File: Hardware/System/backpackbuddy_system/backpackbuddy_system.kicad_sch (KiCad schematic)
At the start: 27 parts, among them J1 PIR, J2 Ultrasonic 2, J3 Ultrasonic 1, J4 Left Vibration 1, J5 Left Vibration 2, J6 Raspberry Pi, J7 ESP8266, J8 Right Vibration 1, J9 Right Vibration 2, Q1 Q_NMOS_GSD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

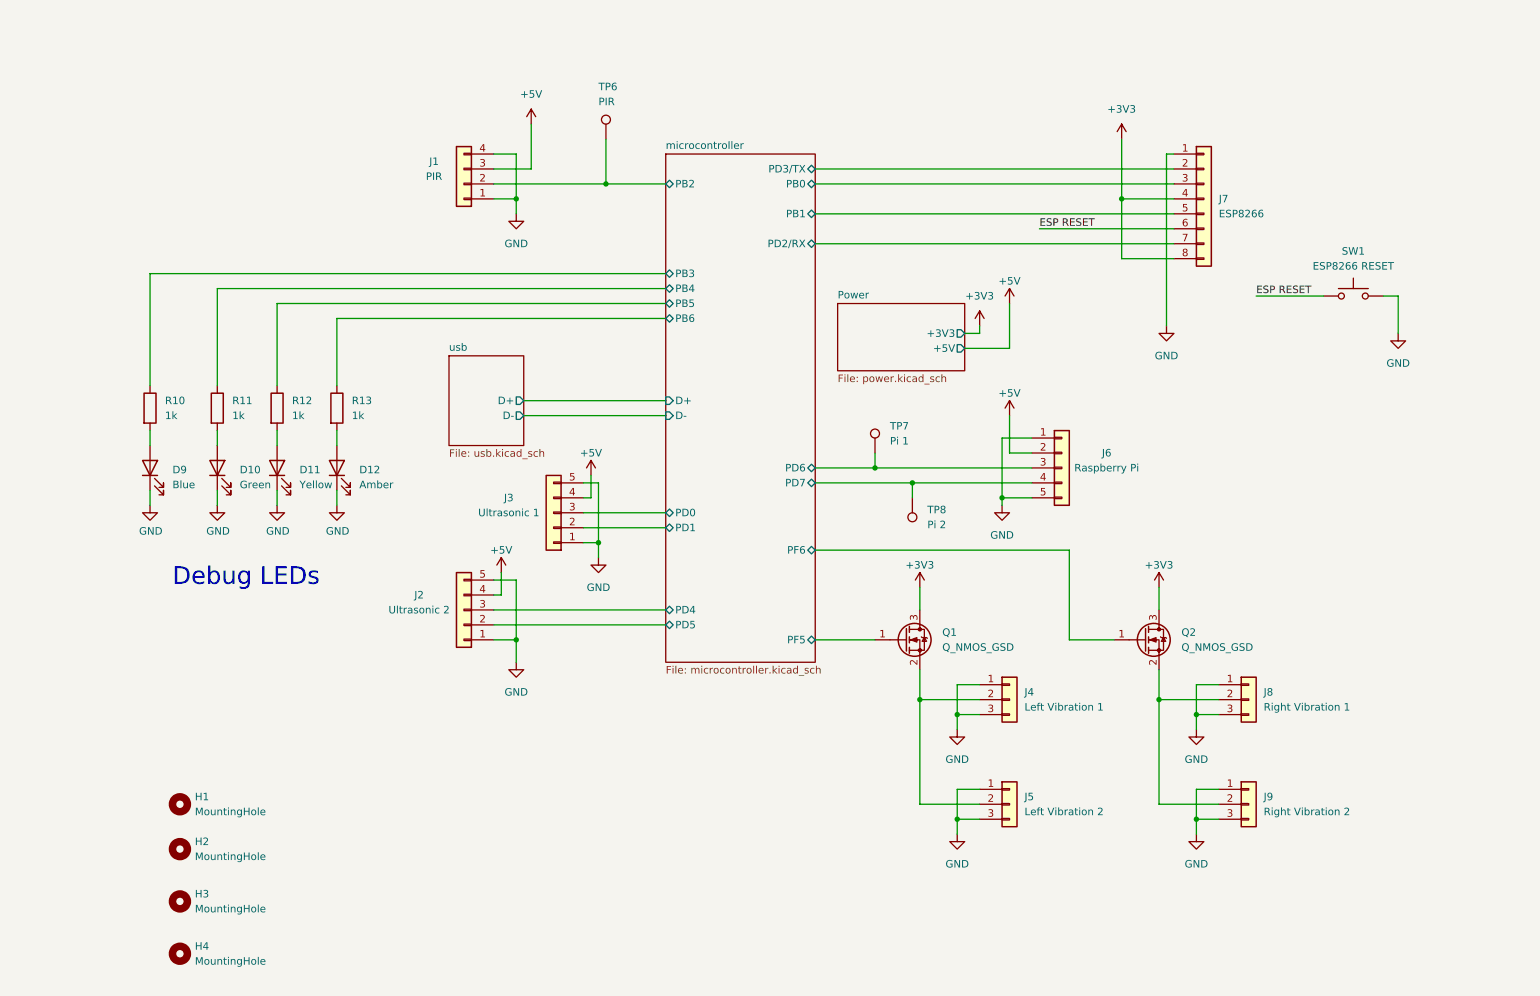
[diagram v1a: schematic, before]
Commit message: about to go crazy with the raspberry pi setup on schematic then will layout after dinner hehe
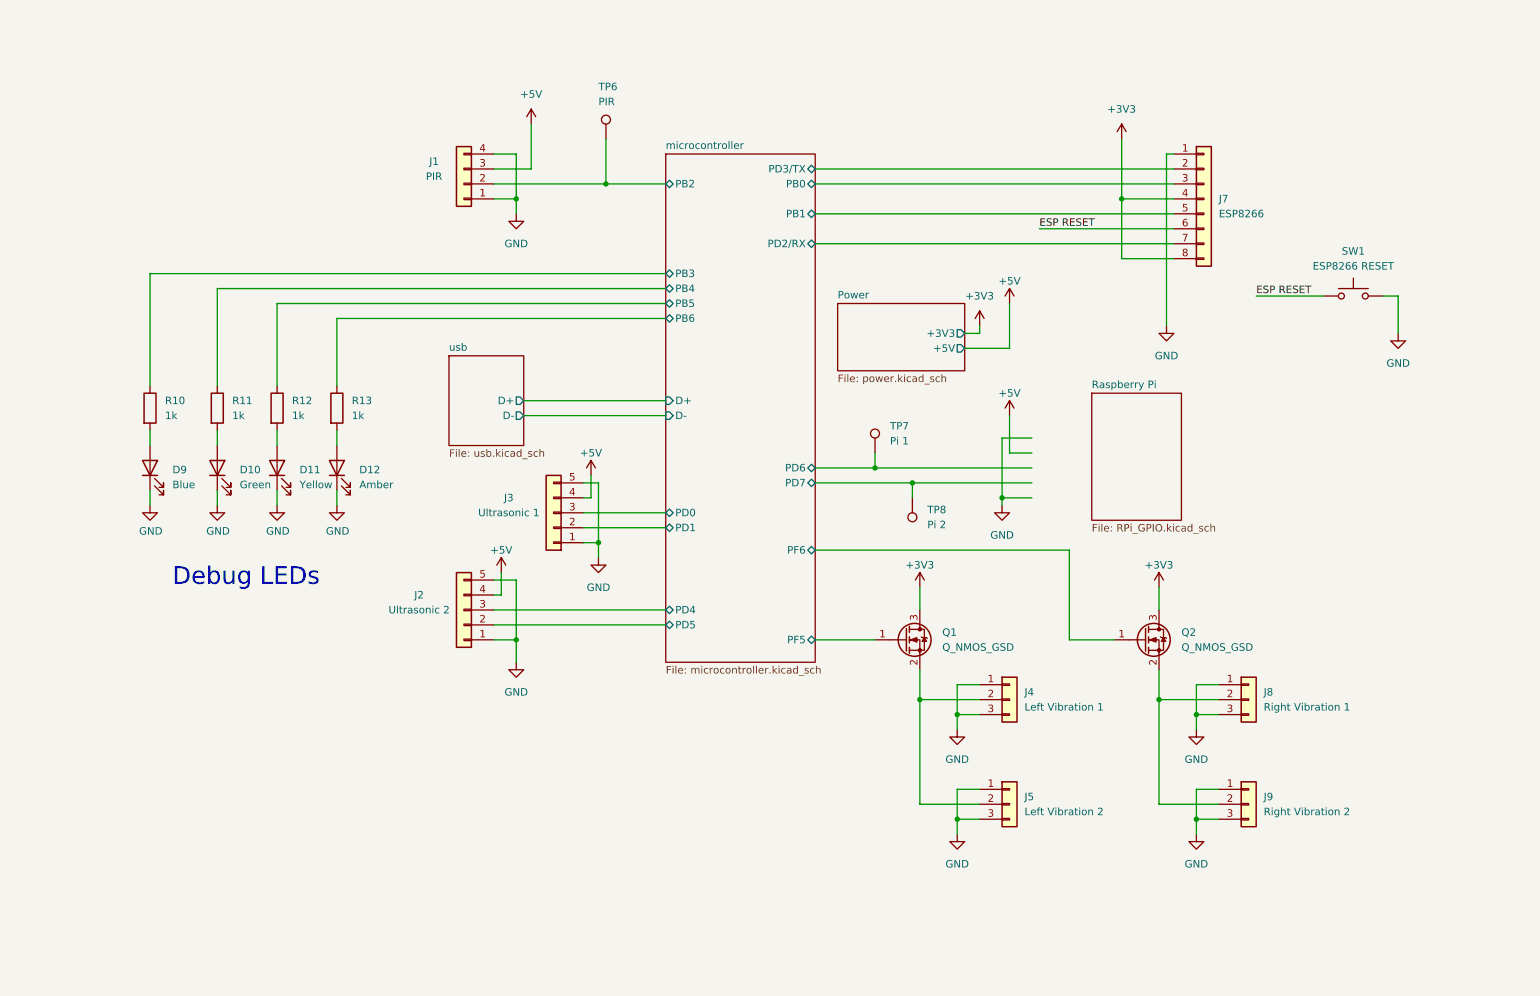
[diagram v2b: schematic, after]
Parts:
- removed H1, H2, H3, H4: MountingHole, MountingHole:MountingHole_2.7mm_M2.5, symbol Mechanical:MountingHole
- removed J6: Raspberry Pi, Connector_PinHeader_2.54mm:PinHeader_1x05_P2.54mm_Vertical, symbol Connector_Generic:Conn_01x05
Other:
- added sheet Raspberry Pi (RPi_GPIO.kicad_sch)
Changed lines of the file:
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@@
     (pin "1")
-  )
-  (symbol (lib_id "Mechanical:MountingHole") (at 49.53 156.21 0) (unit 1)
-    (in_bom yes) (on_board yes) (fields_autoplaced)
-    (property "Reference" "H2" (id 0) (at 52.07 154.9399 0)
-      (effects (font (size 1.27 1.27)) (justify left))
-    )
-    (property "Value" "MountingHole" (id 1) (at 52.07 157.4799 0)
-      (effects (font (size 1.27 1.27)) (justify left))
-    )
-    (property "Footprint" "MountingHole:MountingHole_2.7mm_M2.5" (id 2) (at 49.53 156.21 0)
-      (effects (font (size 1.27 1.27)) hide)
-    )
-    (property "Datasheet" "~" (id 3) (at 49.53 156.21 0)
-      (effects (font (size 1.27 1.27)) hide)
-    )
   )
   (symbol (lib_id "power:GND") (at 66.04 97.79 0) (unit 1)
@@
     (pin "1")
   )
-  (symbol (lib_id "Mechanical:MountingHole") (at 49.53 165.1 0) (unit 1)
-    (in_bom yes) (on_board yes) (fields_autoplaced)
-    (property "Reference" "H3" (id 0) (at 52.07 163.8299 0)
-      (effects (font (size 1.27 1.27)) (justify left))
-    )
-    (property "Value" "MountingHole" (id 1) (at 52.07 166.3699 0)
-      (effects (font (size 1.27 1.27)) (justify left))
-    )
-    (property "Footprint" "MountingHole:MountingHole_2.7mm_M2.5" (id 2) (at 49.53 165.1 0)
-      (effects (font (size 1.27 1.27)) hide)
-    )
-    (property "Datasheet" "~" (id 3) (at 49.53 165.1 0)
-      (effects (font (size 1.27 1.27)) hide)
-    )
-  )
   (symbol (lib_id "Device:R") (at 76.2 81.28 0) (unit 1)
     (in_bom yes) (on_board yes) (fields_autoplaced)
@@
     (pin "1")
   )
-  (symbol (lib_id "Mechanical:MountingHole") (at 49.53 173.99 0) (unit 1)
-    (in_bom yes) (on_board yes) (fields_autoplaced)
-    (property "Reference" "H4" (id 0) (at 52.07 172.7199 0)
-      (effects (font (size 1.27 1.27)) (justify left))
-    )
-    (property "Value" "MountingHole" (id 1) (at 52.07 175.2599 0)
-      (effects (font (size 1.27 1.27)) (justify left))
-    )
-    (property "Footprint" "MountingHole:MountingHole_2.7mm_M2.5" (id 2) (at 49.53 173.99 0)
-      (effects (font (size 1.27 1.27)) hide)
-    )
-    (property "Datasheet" "~" (id 3) (at 49.53 173.99 0)
-      (effects (font (size 1.27 1.27)) hide)
-    )
-  )
   (symbol (lib_id "power:+5V") (at 104.14 109.22 0) (unit 1)
     (in_bom yes) (on_board yes)
@@
     (pin "1")
   )
-  (symbol (lib_id "Mechanical:MountingHole") (at 49.53 148.59 0) (unit 1)
-    (in_bom yes) (on_board yes) (fields_autoplaced)
-    (property "Reference" "H1" (id 0) (at 52.07 147.3199 0)
-      (effects (font (size 1.27 1.27)) (justify left))
-    )
-    (property "Value" "MountingHole" (id 1) (at 52.07 149.8599 0)
-      (effects (font (size 1.27 1.27)) (justify left))
-    )
-    (property "Footprint" "MountingHole:MountingHole_2.7mm_M2.5" (id 2) (at 49.53 148.59 0)
-      (effects (font (size 1.27 1.27)) hide)
-    )
-    (property "Datasheet" "~" (id 3) (at 49.53 148.59 0)
-      (effects (font (size 1.27 1.27)) hide)
-    )
-  )
   (symbol (lib_id "power:GND") (at 181.61 153.67 0) (unit 1)
     (in_bom yes) (on_board yes) (fields_autoplaced)
@@
     )
     (pin "1")
-  )
-  (symbol (lib_id "Connector_Generic:Conn_01x05") (at 199.39 91.44 0) (unit 1)
-    (in_bom yes) (on_board yes)
-    (property "Reference" "J6" (id 0) (at 207.01 88.9 0))
-    (property "Value" "Raspberry Pi" (id 1) (at 207.01 91.44 0))
-    (property "Footprint" "Connector_PinHeader_2.54mm:PinHeader_1x05_P2.54mm_Vertical" (id 2) (at 199.39 91.44 0)
-      (effects (font (size 1.27 1.27)) hide)
-    )
-    (property "Datasheet" "~" (id 3) (at 199.39 91.44 0)
-      (effects (font (size 1.27 1.27)) hide)
-    )
-    (property "Stock" "In connector kit" (id 4) (at 199.39 91.44 0)
-      (effects (font (size 1.27 1.27)) hide)
-    )
-    (pin "1")
-    (pin "2")
-    (pin "3")
-    (pin "4")
-    (pin "5")
   )
   (symbol (lib_id "power:+3V3") (at 215.9 111.76 0) (unit 1)
@@
     )
   )
+  (sheet (at 204.47 78.74) (size 15.24 21.59) (fields_autoplaced)
+    (stroke (width 0.1524) (type solid) (color 0 0 0 0))
+    (fill (color 0 0 0 0.0000))
+    (property "Sheet name" "Raspberry Pi" (id 0) (at 204.47 78.0284 0)
+      (effects (font (size 1.27 1.27)) (justify left bottom))
+    )
+    (property "Sheet file" "RPi_GPIO.kicad_sch" (id 1) (at 204.47 100.9146 0)
+      (effects (font (size 1.27 1.27)) (justify left top))
+    )
+  )
   (sheet (at 95.25 72.39) (size 12.7 15.24) (fields_autoplaced)
     (stroke (width 0.1524) (type solid) (color 0 0 0 0))
@@
     (path "/cf3dbeef-e165-4b09-9181-2cdb640e2044" (page "3"))
     (path "/31ba9691-809e-422e-95e0-c0a31dc5a8d2" (page "4"))
+    (path "/b75bd9b9-3a6b-4766-98aa-3c30f703f2e0" (page "5"))
   )
   (symbol_instances
@@
       (reference "F2") (unit 1) (value "4A") (footprint "Fuse:Fuse_0603_1608Metric_Pad1.05x0.95mm_HandSolder")
     )
-    (path "/7ba4c5ab-53c8-4ed6-a56b-d48ce55bed3f"
-      (reference "H1") (unit 1) (value "MountingHole") (footprint "MountingHole:MountingHole_2.7mm_M2.5")
-    )
-    (path "/2e721548-39f6-4c3c-af59-f1b3c0cd0ccf"
-      (reference "H2") (unit 1) (value "MountingHole") (footprint "MountingHole:MountingHole_2.7mm_M2.5")
-    )
-    (path "/3f16932f-c1ad-452a-a9d6-eed8bdfe8267"
-      (reference "H3") (unit 1) (value "MountingHole") (footprint "MountingHole:MountingHole_2.7mm_M2.5")
-    )
-    (path "/6b7cec68-8bf5-4c72-bd57-d348fd442c4a"
-      (reference "H4") (unit 1) (value "MountingHole") (footprint "MountingHole:MountingHole_2.7mm_M2.5")
-    )
     (path "/e1c39392-4fee-4a21-be8c-0ca37da1cb84"
       (reference "J1") (unit 1) (value "PIR") (footprint "Connector_PinHeader_2.54mm:PinHeader_1x04_P2.54mm_Vertical")
@@
       (reference "J5") (unit 1) (value "Left Vibration 2") (footprint "Connector_PinHeader_2.54mm:PinHeader_1x03_P2.54mm_Vertical")
     )
-    (path "/9f3434b7-25eb-451d-ae48-b1d6349ea6b5"
-      (reference "J6") (unit 1) (value "Raspberry Pi") (footprint "Connector_PinHeader_2.54mm:PinHeader_1x05_P2.54mm_Vertical")
+    (path "/b75bd9b9-3a6b-4766-98aa-3c30f703f2e0/680f5a3d-03b5-4375-afa9-99b8f3b6f5b5"
+      (reference "J6") (unit 1) (value "RPi_GPIO") (footprint "")
     )
     (path "/d8ba2266-3fc9-4f5f-8bd8-53203e01ee14"

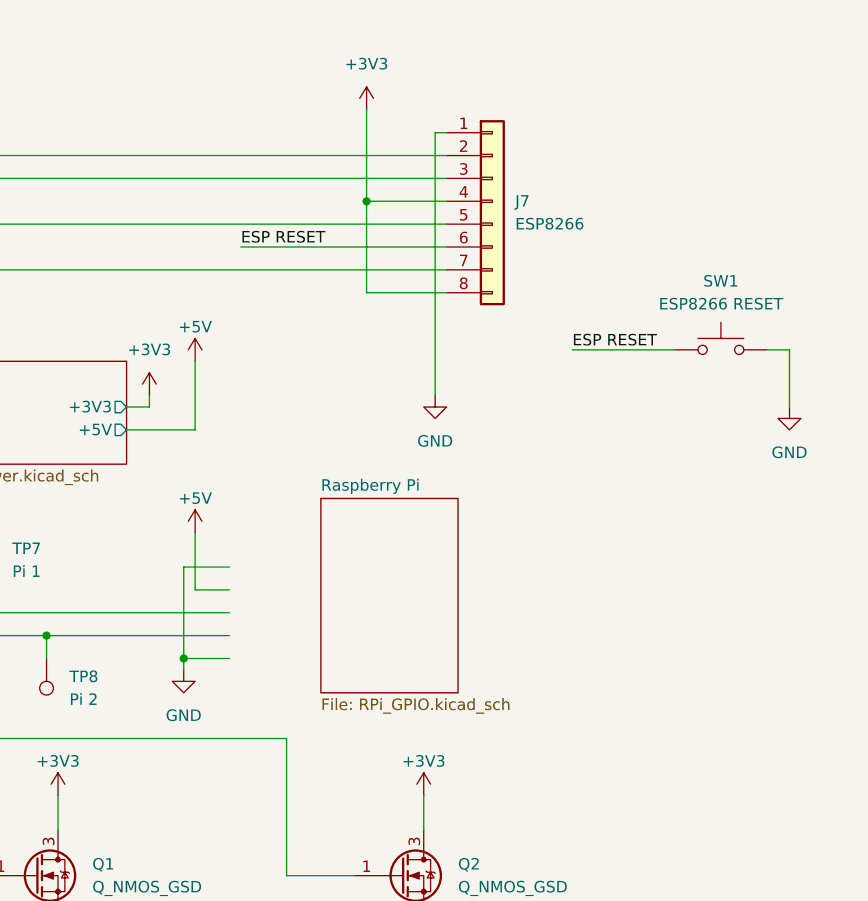
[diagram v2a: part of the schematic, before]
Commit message: pull down resistor to ESP reset
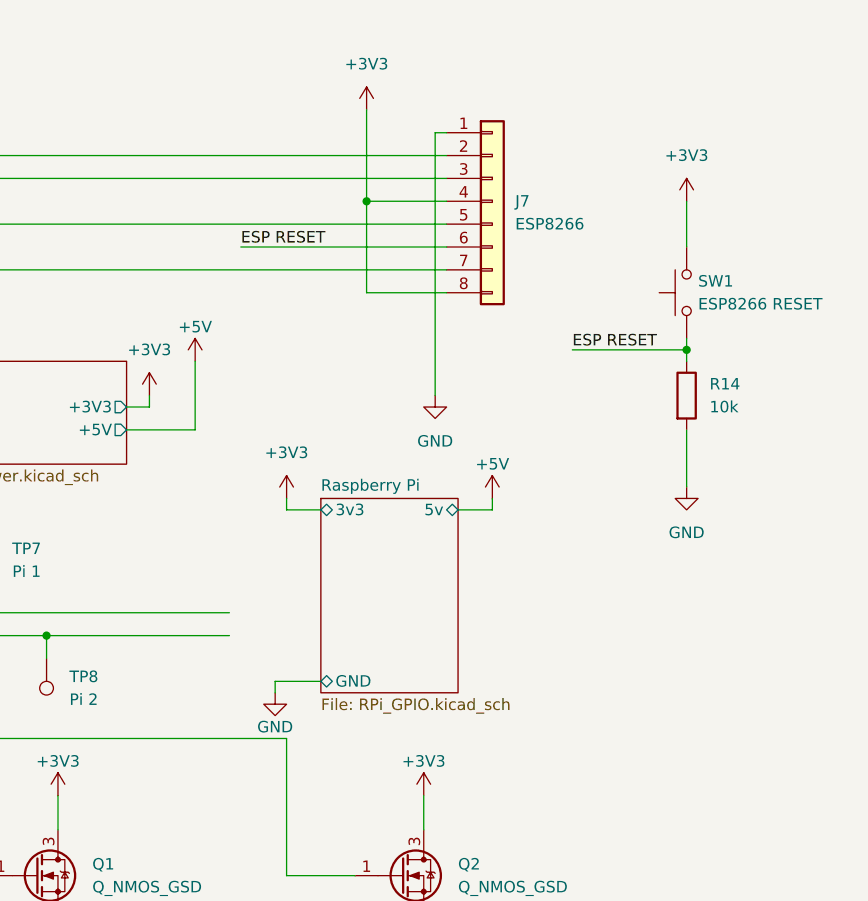
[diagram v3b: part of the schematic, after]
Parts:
- added R14: 10k, Resistor_SMD:R_0603_1608Metric_Pad0.98x0.95mm_HandSolder, symbol Device:R
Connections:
- net +3V3: now also SW1.2
- net ESP RESET: now also R14.1
- net GND: now also R14.2; no longer SW1.2
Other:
- sheet Raspberry Pi ports: added 3v3, 5v, GND; removed none
- moved on the sheet: SW1

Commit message: decoupling caps
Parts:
- added C16, C17, C18, C19: 10uF, Capacitor_SMD:C_0805_2012Metric_Pad1.18x1.45mm_HandSolder, symbol Device:C
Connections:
- net +3V3: now also C19.1
- net +5V: now also C16.1, C17.1, C18.1
- net GND: now also C16.2, C17.2, C18.2, C19.2
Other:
- note added: "SENSOR DECOUPLING CAPS"
